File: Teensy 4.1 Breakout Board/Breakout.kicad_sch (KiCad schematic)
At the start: 16 parts, among them J1 CAN1, J2 CAN2, J3 12V_IN, J4 APPS, J5 BRAKE_PRESSURE_IN, J6 BRAKE_LIGHT_OUT, J7 3.3V_OUT, J8 GND_COMMON, Q1 IRLZ44N, U1 Teensy4.1, U2 MCP2562-E-P, U3 LM2596S-5, U4 MCP2562-E-P

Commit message: Keelan Test
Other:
- note added: "Keelan Test"
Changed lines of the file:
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@@
 	(generator_version "9.0")
 	(paper "A4")
+	(text "Keelan Test"
+		(exclude_from_sim no)
+		(at 222.758 54.61 0)
+		(effects
+			(font
+				(size 1.27 1.27)
+			)
+		)
+	)
 	(junction
 		(at 163.83 26.67)

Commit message: breakout board v1 sizing
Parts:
- removed J1: CAN1, TerminalBlock_Phoenix:TerminalBlock_Phoenix_MKDS-1,5-2-5.08_1x02_P5.08mm_Horizontal, symbol Connector:Screw_Terminal_01x02
- removed J2: CAN2, TerminalBlock_Phoenix:TerminalBlock_Phoenix_MKDS-1,5-2-5.08_1x02_P5.08mm_Horizontal, symbol Connector:Screw_Terminal_01x02
- removed J3: 12V_IN, TerminalBlock_Phoenix:TerminalBlock_Phoenix_MKDS-1,5-2-5.08_1x02_P5.08mm_Horizontal, symbol Connector:Screw_Terminal_01x02
- removed J4: APPS, TerminalBlock_Phoenix:TerminalBlock_Phoenix_MKDS-1,5-2-5.08_1x02_P5.08mm_Horizontal, symbol Connector:Screw_Terminal_01x02
- removed J5: BRAKE_PRESSURE_IN, TerminalBlock_Phoenix:TerminalBlock_Phoenix_MKDS-1,5-2-5.08_1x02_P5.08mm_Horizontal, symbol Connector:Screw_Terminal_01x02
- removed J6: BRAKE_LIGHT_OUT, TerminalBlock_Phoenix:TerminalBlock_Phoenix_MKDS-1,5-2-5.08_1x02_P5.08mm_Horizontal, symbol Connector:Screw_Terminal_01x02
- removed J7: 3.3V_OUT, TerminalBlock_Phoenix:TerminalBlock_Phoenix_MKDS-1,5-4-5.08_1x04_P5.08mm_Horizontal, symbol Connector:Screw_Terminal_01x04
- removed J8: GND_COMMON, TerminalBlock_Phoenix:TerminalBlock_Phoenix_MKDS-1,5-4-5.08_1x04_P5.08mm_Horizontal, symbol Connector:Screw_Terminal_01x04
- removed Q1: IRLZ44N, Package_TO_SOT_THT:TO-220-3_Vertical, symbol Transistor_FET:IRLZ44N
- removed U1: Teensy4.1, teensy:Teensy41, symbol teensy:Teensy4.1
- removed U2, U4: MCP2562-E-P, Package_DIP:DIP-8_W7.62mm, symbol Interface_CAN_LIN:MCP2562-E-P
- removed U3: LM2596S-5, Package_TO_SOT_SMD:TO-263-5_TabPin3, symbol Regulator_Switching:LM2596S-5
- added C1, C2, C3, C5, C6, C7, C8: 0.1uF, FA14_Capacitor:FA18X7R1H104KNU00, symbol Device:C
- added C15: 220uF, Capacitor_THT:CP_Radial_D6.3mm_P2.50mm, symbol Device:C_Polarized
- added C18: 680uF, footprints:CAPPRD500W60D1275H2700, symbol 50ZLJ680M12_5X25:50ZLJ680M12.5X25
- added C9: 10uF, Capacitor_THT:CP_Radial_D5.0mm_P2.50mm, symbol Device:C_Polarized
- added D1: NUP3105L, Package_TO_SOT_SMD:SOT-23, symbol Power_Protection:NUP2105L
- added D3: 1N5821, Diode_THT:D_DO-201AD_P15.24mm_Horizontal, symbol Diode:1N5821
- added J1: CAN, Connector_JST:JST_XH_B3B-XH-A_1x03_P2.50mm_Vertical, symbol Connector_Generic:Conn_01x03
- added J10: RTD_Speaker, Connector_JST:JST_XH_B2B-XH-A_1x02_P2.50mm_Vertical, symbol Connector_Generic:Conn_01x02
- added J2: 12V Power, Connector_JST:JST_XH_B2B-XH-A_1x02_P2.50mm_Vertical, symbol Connector_Generic:Conn_01x02
- added J3: APPS1, Connector_JST:JST_XH_B3B-XH-A_1x03_P2.50mm_Vertical, symbol Connector_Generic:Conn_01x03
- added J4: APPS2, Connector_JST:JST_XH_B3B-XH-A_1x03_P2.50mm_Vertical, symbol Connector_Generic:Conn_01x03
- added J5: Brake_Pressure_Front, Connector_JST:JST_XH_B3B-XH-A_1x03_P2.50mm_Vertical, symbol Connector_Generic:Conn_01x03
- added J6: Brake_Pressure_Rear, Connector_JST:JST_XH_B3B-XH-A_1x03_P2.50mm_Vertical, symbol Connector_Generic:Conn_01x03
- added J7: Nextion, Connector_JST:JST_XH_B4B-XH-A_1x04_P2.50mm_Vertical, symbol Connector_Generic:Conn_01x04
- added J8: ESP32, Connector_JST:JST_XH_B4B-XH-A_1x04_P2.50mm_Vertical, symbol Connector_Generic:Conn_01x04
- added J9: Brake_Light, Connector_JST:JST_XH_B2B-XH-A_1x02_P2.50mm_Vertical, symbol Connector_Generic:Conn_01x02
- added JP1: SolderJumper_2_Open, Jumper:SolderJumper-2_P1.3mm_Open_Pad1.0x1.5mm, symbol Jumper:SolderJumper_2_Open
- added L1: 33uH, Inductor_SMD:L_10.4x10.4_H4.8, symbol Device:L
- added Q1, Q2: 2N7000, Package_TO_SOT_THT:TO-92_Inline, symbol Transistor_FET:2N7000
- added R10, R12, R4: 20k, Resistor_THT:R_Axial_DIN0207_L6.3mm_D2.5mm_P10.16mm_Horizontal, symbol Device:R
- added R11, R9: 10k, Resistor_THT:R_Axial_DIN0207_L6.3mm_D2.5mm_P10.16mm_Horizontal, symbol Device:R
- added R13, R14, R15, R16: 1k, Resistor_THT:R_Axial_DIN0207_L6.3mm_D2.5mm_P10.16mm_Horizontal, symbol Device:R
- added R5, R7: 100, Resistor_THT:R_Axial_DIN0207_L6.3mm_D2.5mm_P10.16mm_Horizontal, symbol Device:R
- added R6, R8: 100k, Resistor_THT:R_Axial_DIN0207_L6.3mm_D2.5mm_P10.16mm_Horizontal, symbol Device:R
- added R_CAN_TERM1: 120, Resistor_THT:R_Axial_DIN0207_L6.3mm_D2.5mm_P10.16mm_Horizontal, symbol Device:R
- added U1: SN65HVD230, Package_SO:SOIC-8_3.9x4.9mm_P1.27mm, symbol Interface_CAN_LIN:SN65HVD230
- added U2: module_mpu6050, usini_sensors:module_mpu6050, symbol usini_sensors:module_mpu6050
- added U26: LM2596SX-5.0/NOPB, Package_TO_SOT_SMD:TO-263-5_TabPin3, symbol Regulator_Switching:LM2596S-5
- added U3: Teensy4.1, teensy.pretty-master:Teensy41, symbol teensy:Teensy4.1
- R1: value 120 -> 10k; footprint Resistor_SMD:R_0603_1608Metric -> Resistor_THT:R_Axial_DIN0207_L6.3mm_D2.5mm_P10.16mm_Horizontal; Part Number (none) -> MCF 0.25W 10K
- R2: value 120 -> 20k; footprint Resistor_SMD:R_0603_1608Metric -> Resistor_THT:R_Axial_DIN0207_L6.3mm_D2.5mm_P10.16mm_Horizontal; Part Number (none) -> CFR25SJT-52A20K
- R3: value 10K -> 10k; footprint Resistor_SMD:R_0603_1608Metric -> Resistor_THT:R_Axial_DIN0207_L6.3mm_D2.5mm_P10.16mm_Horizontal; Part Number (none) -> MCF 0.25W 10K
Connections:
- net 3.3V: now also C1.2, C2.2, U1.3 (VCC), U2.1 (VCC), U3.46 (3V3)
- net 5V: now also C15.1, C3.2, C9.1, J3.1 (Pin_1), J4.1 (Pin_1), J5.1 (Pin_1), J6.1 (Pin_1), J7.1 (Pin_1), J8.1 (Pin_1), L1.2, U26.4 (FB), U3.48 (VIN)
- net APPS1: now also R1.1, J3.2 (Pin_2)
- net APPS2: now also R3.1, J4.2 (Pin_2)
- net CAN1_RX: now also U1.4 (R), U3.45 (23_A9_CRX1_MCLK1)
- net CAN1_TX: now also U1.1 (D), U3.44 (22_A8_CTX1)
- net GND: now also R2.2, C1.1, C15.2, C18.2 (-), C2.1, C3.1, C5.2, C6.2, C7.2, C8.2, C9.2, D1.3 (A), D3.2 (A), J1.1 (Pin_1), J2.2 (Pin_2), J3.3 (Pin_3), J4.3 (Pin_3), J5.3 (Pin_3), J6.3 (Pin_3), J7.4 (Pin_4), J8.4 (Pin_4), Q1.1 (S), Q2.1 (S), R10.2, R12.2, R4.2, R6.1, R8.1, U1.2 (GND), U1.8 (Rs), U2.2 (GND), U26.3 (GND), U26.5 (~{ON}/OFF), U3.47 (GND); no longer R3.1
- net at R2.1: now also R1.2, R13.2
- net BRAKE_LIGHT_CONTROL: no longer names the net of R3.2
- net BRAKE_LIGHT_CONTROL: now also R14.2, R4.1
- new net: Q1.2 (G), R5.2, R6.2
- new net: Q2.2 (G), R7.2, R8.2
- new net: JP1.2 (B), R_CAN_TERM1.2
- new net: D3.1 (K), L1.1, U26.2 (OUT)
- new net: R11.2, R12.1, R16.2
- new net: R10.1, R15.2, R9.2
- new net: J9.2 (Pin_2), Q1.3 (D)
- new net: J10.2 (Pin_2), Q2.3 (D)
- new net 12V: C18.1 (+), J10.1 (Pin_1), J2.1 (Pin_1), J9.1 (Pin_1), U26.1 (VIN)
- new net APPS1_3.3V: C5.1, R13.1, U3.36 (14_A0_TX3_SPDIF_OUT)
- new net APPS2_3.3V: C6.1, R14.1, U3.37 (15_A1_RX3_SPDIF_IN)
- new net Brake_Front: J5.2 (Pin_2), R9.1
- new net Brake_Front_3.3V: C7.1, R15.1, U3.38 (16_A2_RX4_SCL1)
- new net Brake_Light_EN: R5.1, U3.8 (6_OUT1D)
- new net Brake_Rear: J6.2 (Pin_2), R11.1
- new net Brake_Rear_3.3V: C8.1, R16.1, U3.39 (17_A3_TX4_SDA1)
- new net CANH: D1.1 (K), J1.3 (Pin_3), R_CAN_TERM1.1, U1.7 (CANH)
- new net CANL: D1.2 (K), J1.2 (Pin_2), JP1.1 (A), U1.6 (CANL)
- new net ESP32_RX: J8.3 (Pin_3), U3.10 (8_TX2_IN1)
- new net ESP32_TX: J8.2 (Pin_2), U3.9 (7_RX2_OUT1A)
- new net MPU_SCL: U2.3 (SCL), U3.41 (19_A5_SCL)
- new net MPU_SDA: U2.4 (SDA), U3.40 (18_A4_SDA)
- new net Nextion_RX: J7.3 (Pin_3), U3.3 (1_TX1_CTX2_MISO1)
- new net Nextion_TX: J7.2 (Pin_2), U3.2 (0_RX1_CRX2_CS1)
- new net RTD_Speaker_EN: R7.1, U3.11 (9_OUT1C)
- no-connect marks 1 -> 2
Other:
- note added: "120 Ω CAN termination Populate only if this PCB is end-of-bus"
- note added: "Analogue Sensors"
- note added: "Assuming M7100, and scaling down to 3.3V"
- note added: "Brake Light and Speaker"
- note added: "Buck Converter"
- note added: "CAN TVS Protection Diode"
- note added: "CAN Transceiver"
- note added: "Consider replacing for synchronous buck and different output based on current requirements"
- note added: "ESP32 TX to Teensy RX Teensy TX to ESP32 RX"
- note added: "LP Filter should be physically close to Teensy"
- note added: "MPU Sensor"
- note added: "Nextion TX to Teensy RX Teensy TX to Nextion RX"
- note added: "Pin 1: Red wire Pin 2: Black Wire"
- note added: "RS to GND for High Speed mode"
- note added: "Serial 1"
- note added: "Serial 2"
- note added: "Teensy 4.1 Microcontroller"
- note added: "UART Interface"
- note added: "VIN and VUSB link on Teensy 4.1 should be cut to avoid back-feeding"
- note added: "Will be mounted on socket 2x24 and some others"
- note added: "all ADC signals need a return ground to prevent ground offset and jitter. Ground locally at chassis is not a good idea"
- note added: "buck converter"
- note added: "check current"
- note added: "no pull up resistors necessary for adafruit mpu6050"
- note added: "probably need more input protection"
- note removed: "Keelan Test"

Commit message: breakout complete
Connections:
- net CANH: now also J1.2 (Pin_2); no longer J1.3 (Pin_3)
- net CANL: now also J1.3 (Pin_3); no longer J1.2 (Pin_2)

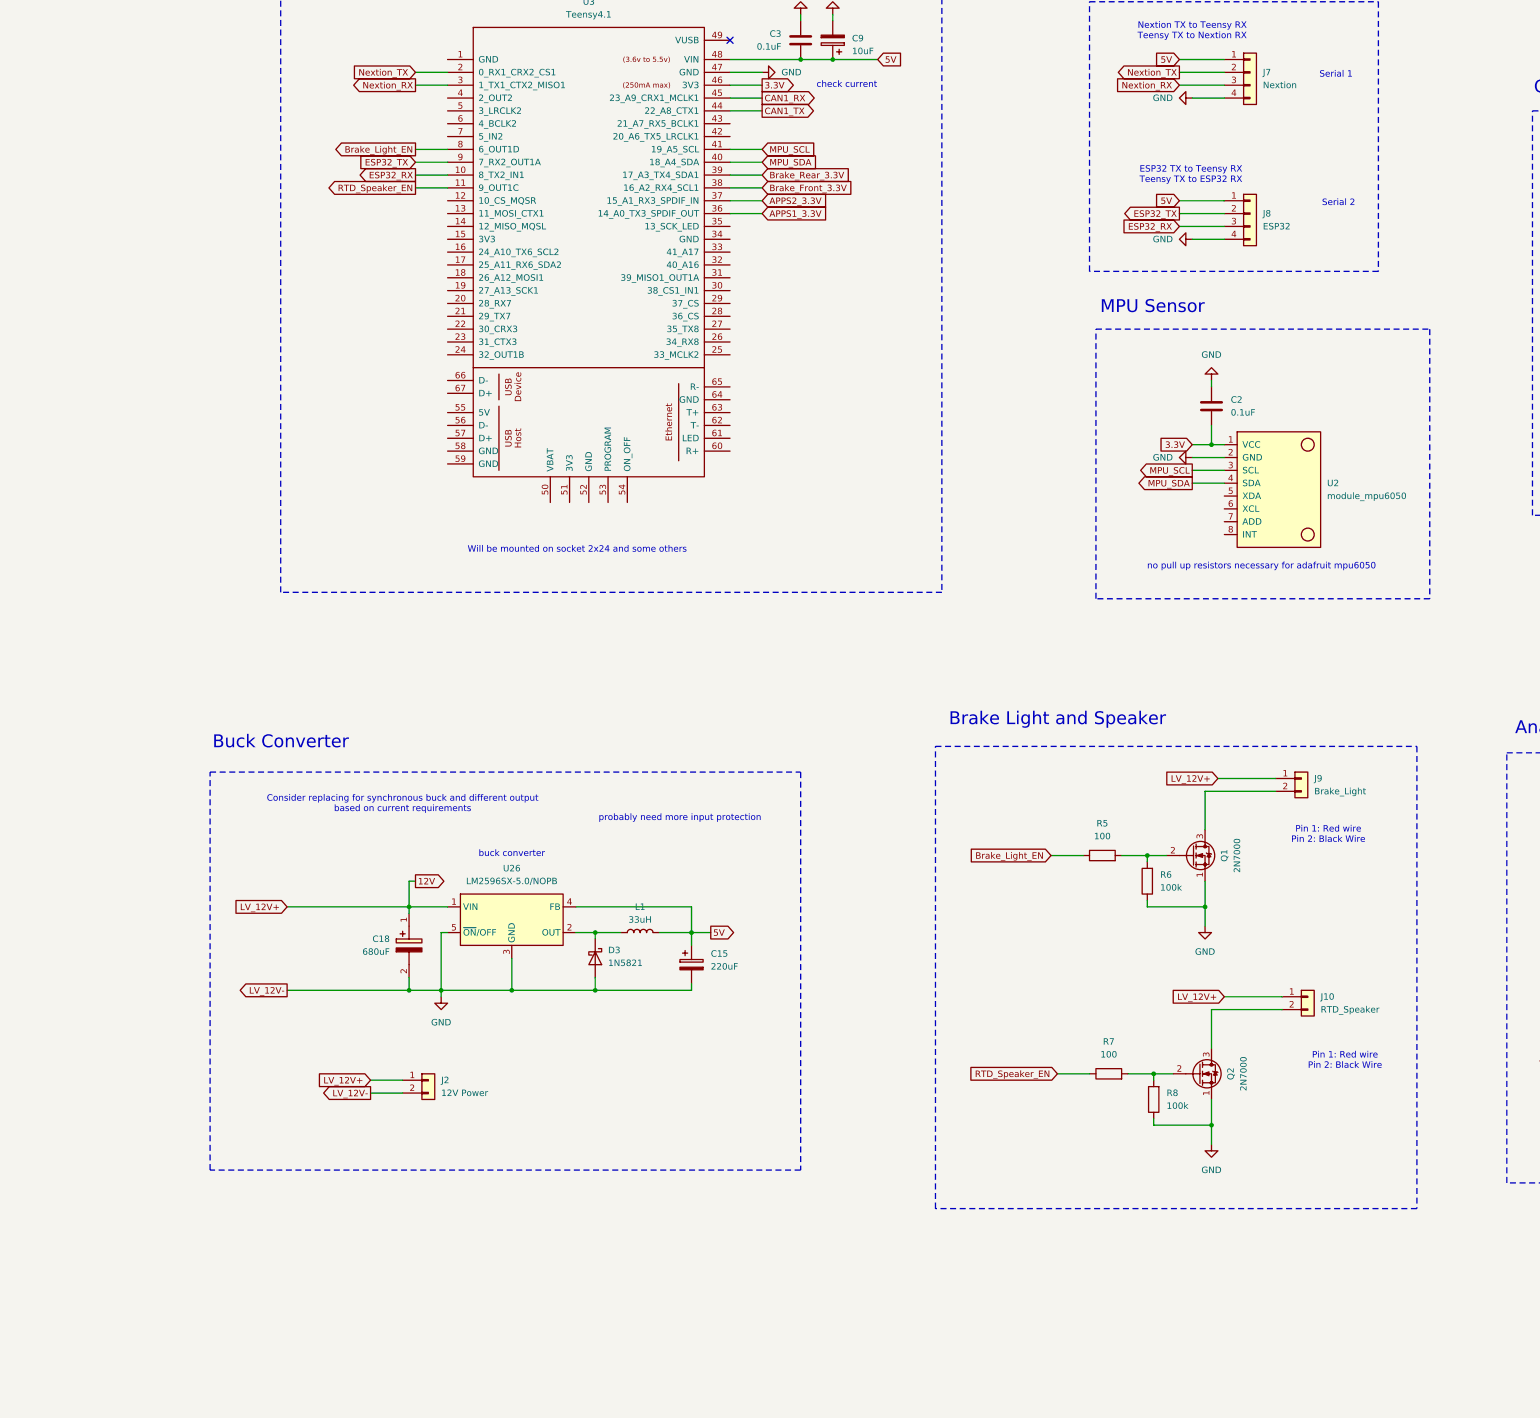
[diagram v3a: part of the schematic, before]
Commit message: breakout updated and ENNOID BMS added
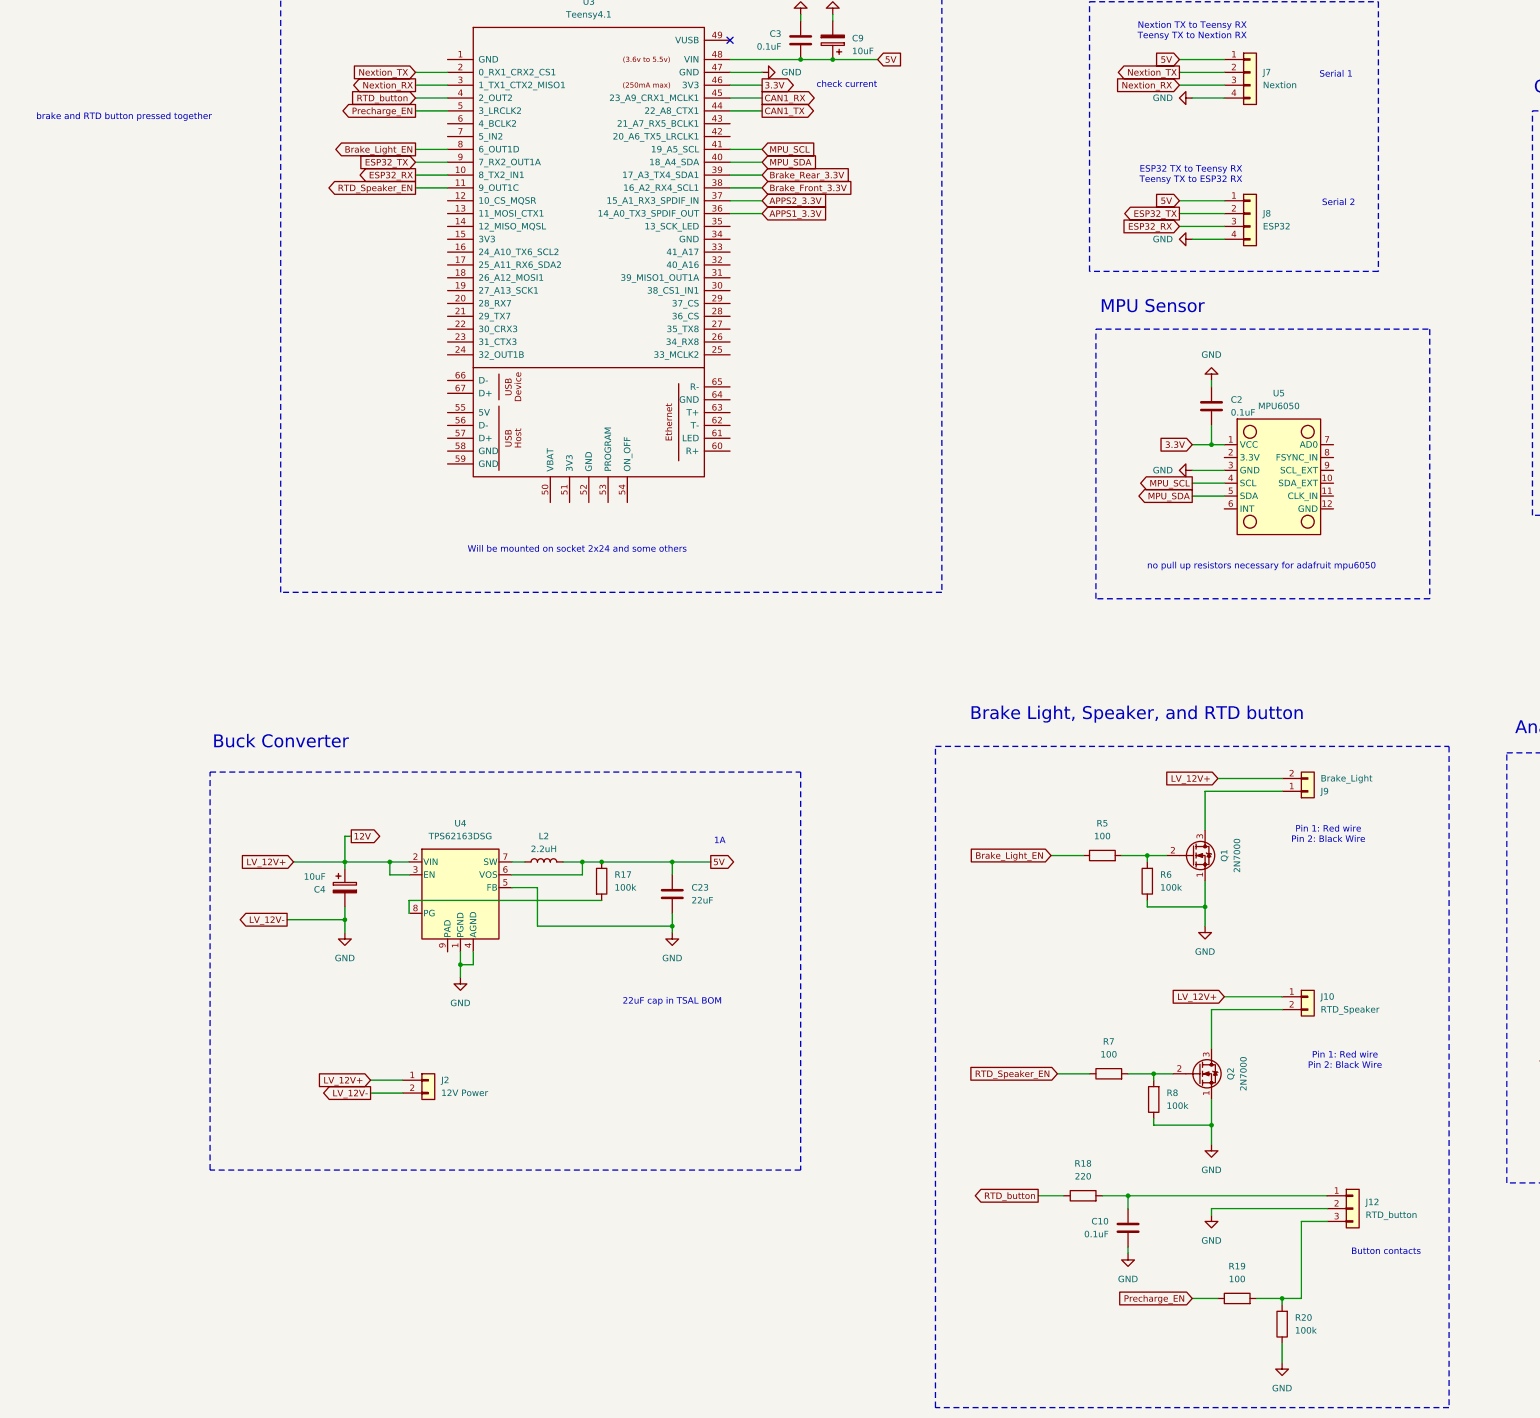
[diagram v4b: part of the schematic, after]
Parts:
- removed C15: 220uF, Capacitor_THT:CP_Radial_D6.3mm_P2.50mm, symbol Device:C_Polarized
- removed C18: 680uF, footprints:CAPPRD500W60D1275H2700, symbol 50ZLJ680M12_5X25:50ZLJ680M12.5X25
- removed D3: 1N5821, Diode_THT:D_DO-201AD_P15.24mm_Horizontal, symbol Diode:1N5821
- removed L1: 33uH, Inductor_SMD:L_10.4x10.4_H4.8, symbol Device:L
- removed U2: module_mpu6050, usini_sensors:module_mpu6050, symbol usini_sensors:module_mpu6050
- removed U26: LM2596SX-5.0/NOPB, Package_TO_SOT_SMD:TO-263-5_TabPin3, symbol Regulator_Switching:LM2596S-5
- added C10: 0.1uF, FA14_Capacitor:FA18X7R1H104KNU00, symbol Device:C
- added C23: 22uF, RDEC71E:RDEC71E226K3P1H03B, symbol Device:C
- added C4: 10uF, Capacitor_THT:CP_Radial_D5.0mm_P2.50mm, symbol Device:C_Polarized
- added J12: RTD_button, Connector_JST:JST_XH_B3B-XH-A_1x03_P2.50mm_Vertical, symbol Connector_Generic:Conn_01x03
- added L2: 2.2uH, XFL3012222:XFL3012222MEC, symbol Device:L
- added R17, R20: 100k, Resistor_THT:R_Axial_DIN0207_L6.3mm_D2.5mm_P10.16mm_Horizontal, symbol Device:R
- added R18: 220, Resistor_THT:R_Axial_DIN0207_L6.3mm_D2.5mm_P10.16mm_Horizontal, symbol Device:R
- added R19: 100, Resistor_THT:R_Axial_DIN0207_L6.3mm_D2.5mm_P10.16mm_Horizontal, symbol Device:R
- added U4: TPS62163DSG, Package_SON:WSON-8-1EP_2x2mm_P0.5mm_EP0.9x1.6mm_ThermalVias, symbol Regulator_Switching:TPS62163DSG
- added U5: MPU6050, adafruit:MPU6050, symbol Adafruit:MPU6050
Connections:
- net 12V: now also J9.2 (Pin_2), C4.1, U4.2 (VIN), U4.3 (EN); no longer J9.1 (Pin_1)
- net 3.3V: now also U5.1 (VCC)
- net 5V: now also C23.2, L2.2, R17.1, U4.6 (VOS)
- net GND: now also C10.2, C23.1, C4.2, J12.2 (Pin_2), R20.1, U4.1 (PGND), U4.4 (AGND), U4.5 (FB), U5.3 (GND)
- net MPU_SCL: now also U5.4 (SCL)
- net MPU_SDA: now also U5.5 (SDA)
- net RTD_button: now reaches U3.4 (2_OUT2)
- net RTD_button: now also R18.1
- net Precharge_EN: now reaches U3.5 (3_LRCLK2)
- net Precharge_EN: now also R19.1
- net at Q1.3 (D): now also J9.1 (Pin_1); no longer J9.2 (Pin_2)
- new net: R17.2, U4.8 (PG)
- new net: L2.1, U4.7 (SW)
- new net: J12.3 (Pin_3), R19.2, R20.2
- new net: C10.1, J12.1 (Pin_1), R18.2
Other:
- note added: "1A"
- note added: "22uF cap in TSAL BOM"
- note added: "Brake Light, Speaker, and RTD button"
- note added: "Button contacts"
- note added: "brake and RTD button pressed together"
- note removed: "Brake Light and Speaker"
- note removed: "Consider replacing for synchronous buck and different output based on current requirements"
- note removed: "buck converter"
- note removed: "probably need more input protection"
- moved on the sheet: J9
